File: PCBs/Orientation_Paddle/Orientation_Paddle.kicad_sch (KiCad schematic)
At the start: 46 parts

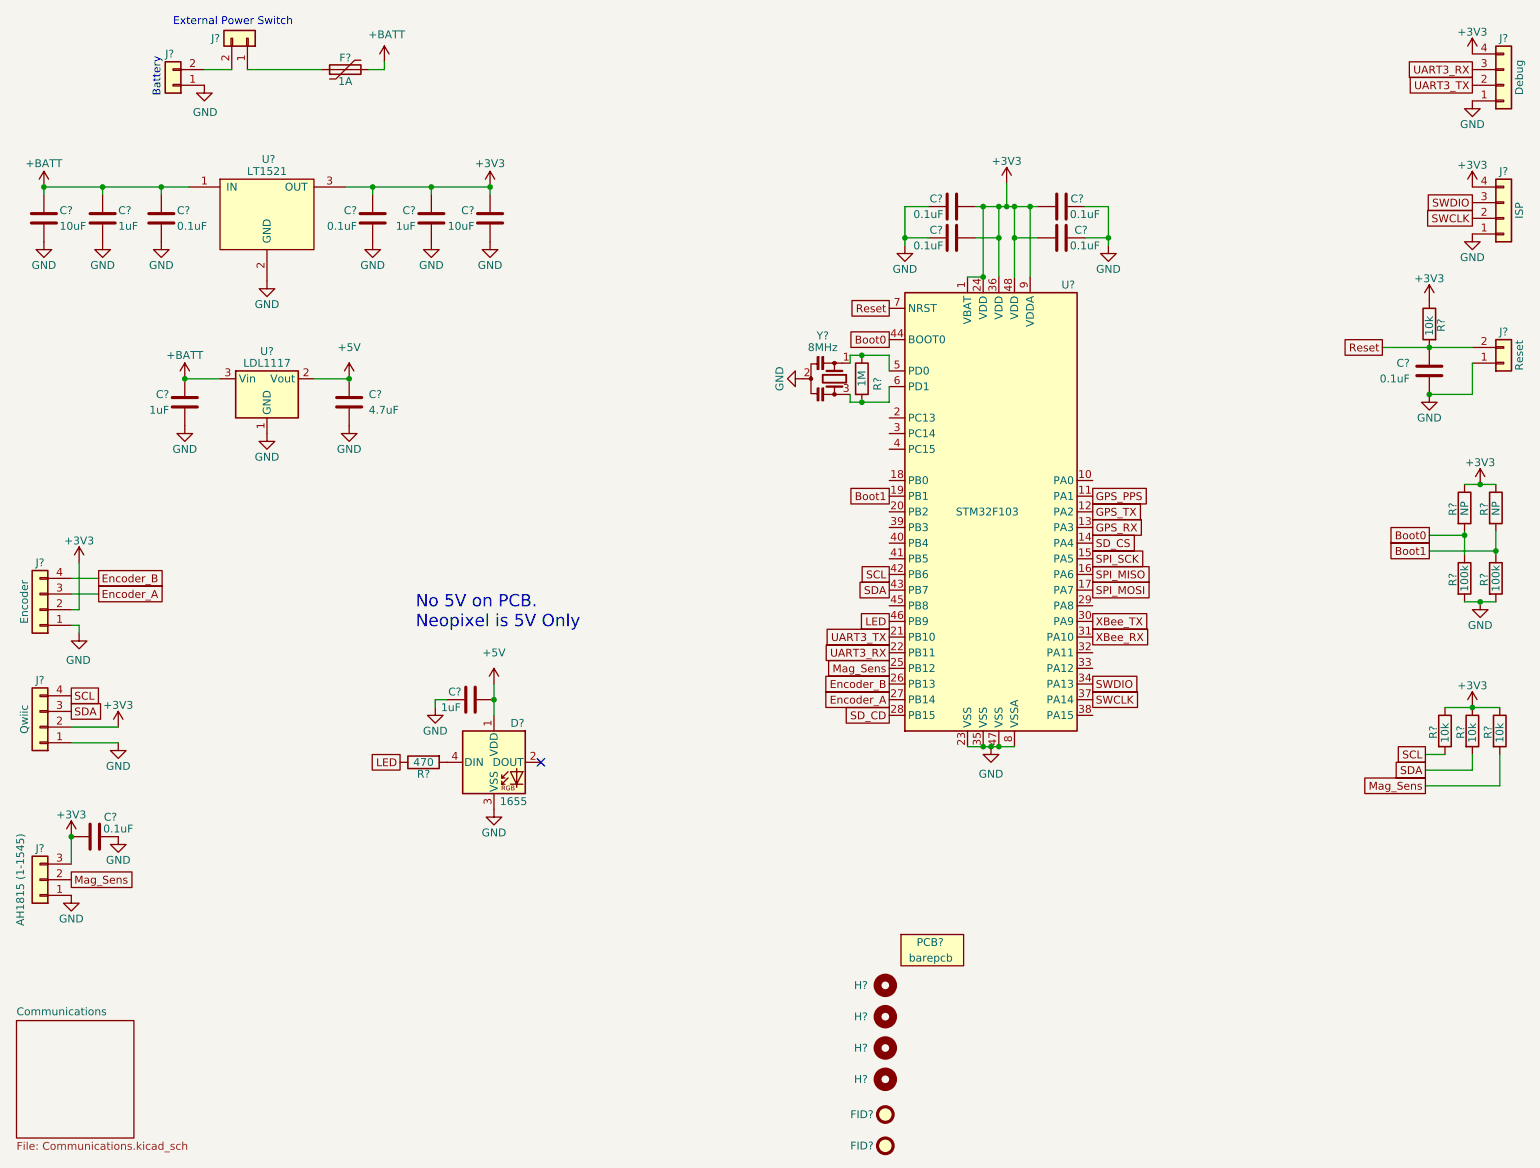
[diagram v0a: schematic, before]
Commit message: Updated Ori. Paddle Schematic with Final Revisions
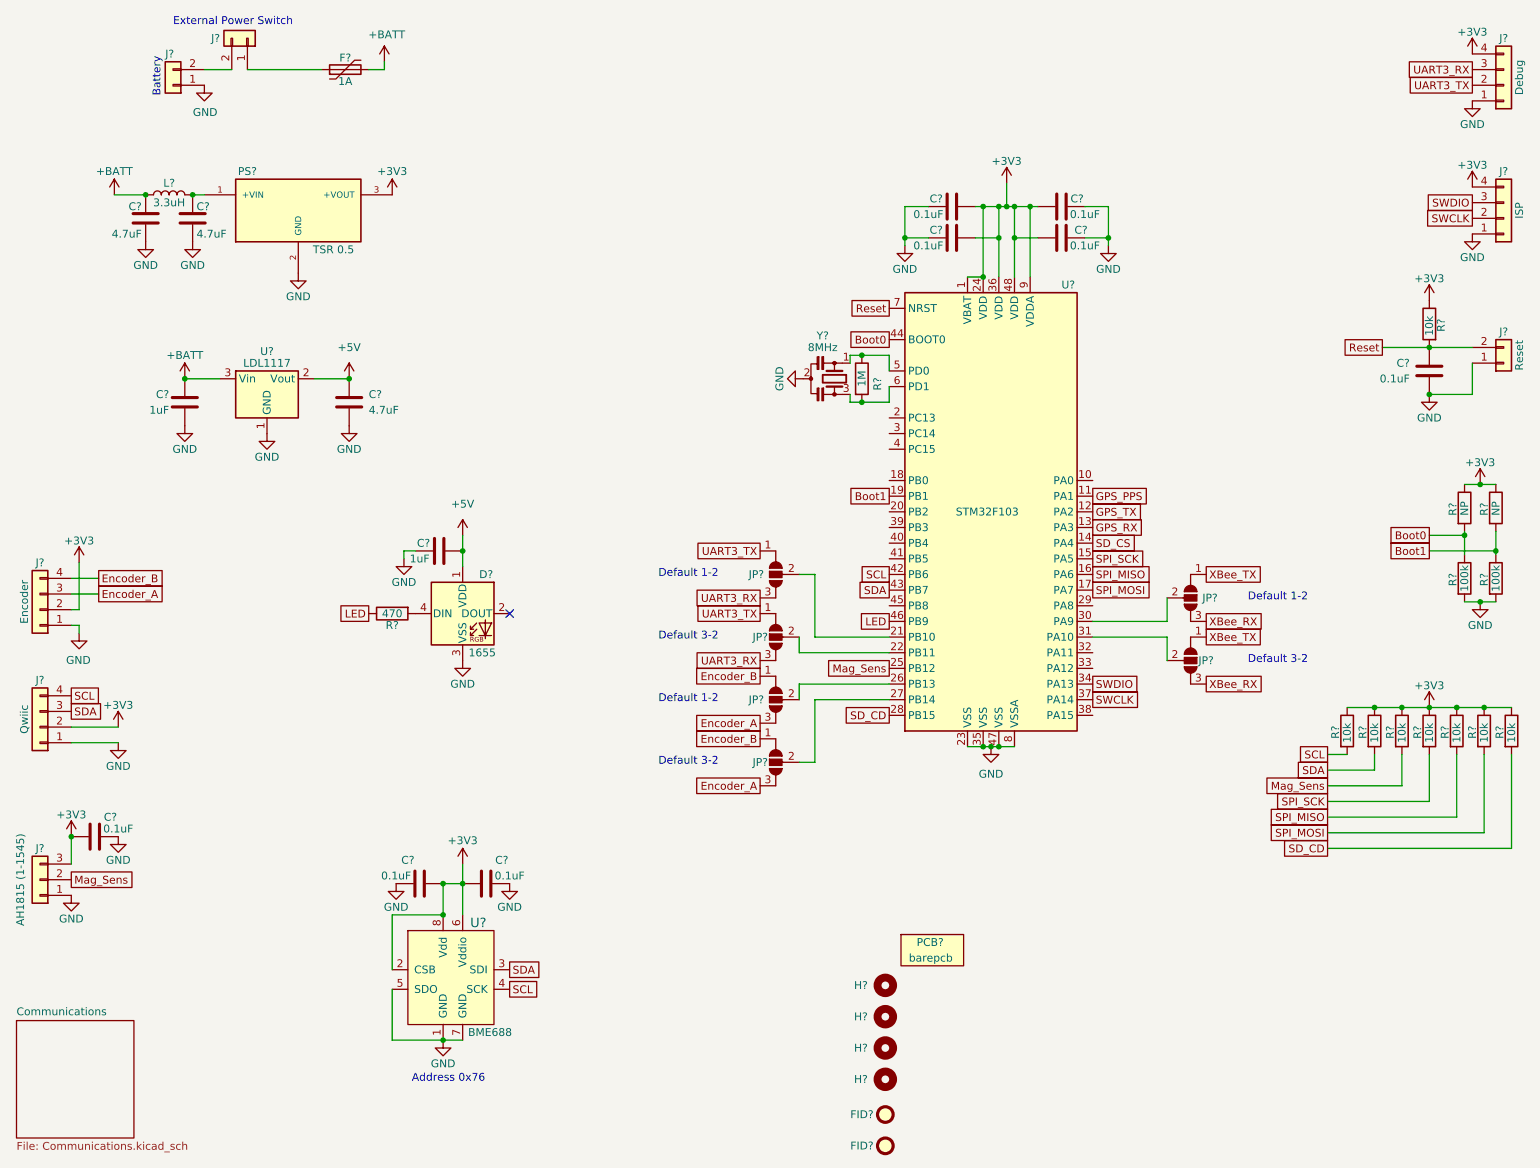
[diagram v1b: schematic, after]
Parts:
- removed C? (x2): 1-0000007, capacitors_0603:1-0000007, symbol capacitors_0603:1-0000007
- removed C? (x2): 1-0000005, capacitors_0603:1-0000005, symbol capacitors_0603:1-0000005
- removed C? (x2): 1-0000018, capacitors_0603:1-0000018, symbol capacitors_0603:1-0000018
- removed U?: 1-0000196, regulators:1-0000196, symbol regulators:1-0000196
- added C? (x2): 1-0000136, capacitors_1206:1-0000136, symbol capacitors_1206:1-0000136
- added C? (x2): 1-0000007, capacitors_0603:1-0000007, symbol capacitors_0603:1-0000007
- added JP? (x6): SolderJumper_3_Open, Jumper:SolderJumper-3_P1.3mm_Open_RoundedPad1.0x1.5mm_NumberLabels, symbol Jumper:SolderJumper_3_Open
- added L?: 1-0000931, inductors:1-0000931, symbol inductors:1-0000931
- added PS?: 1-0000727, dc_dc_converters:1-0000727, symbol dc_dc_converters:1-0000727
- added R? (x4): 1-0000010, resistors_0603:1-0000010, symbol resistors_0603:1-0000010
- added U?: 1-0001471, sensors:1-0001471, symbol sensors:1-0001471
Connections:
- net +3V3: now also C?.1, C?.2, PS?.3 (+VOUT), R?.1, R?.1, R?.1, R?.1, U?.2 (CSB), U?.6 (Vddio), U?.8 (Vdd)
- net +BATT: now also C?.1, L?.1
- net Encoder_A: now also JP?.3 (B), JP?.3 (B); no longer U?.27 (PB14)
- net Encoder_B: now also JP?.1 (A), JP?.1 (A); no longer U?.26 (PB13)
- net GND: now also C?.1, C?.2, C?.2, C?.2, PS?.2 (GND), U?.1 (GND), U?.5 (SDO), U?.7 (GND)
- net SCL: now also U?.4 (SCK)
- net SDA: now also U?.3 (SDI)
- net SD_CD: now also R?.2
- net SPI_MISO: now also R?.2
- net SPI_MOSI: now also R?.2
- net SPI_SCK: now also R?.2
- net UART3_RX: now also JP?.3 (B), JP?.3 (B); no longer U?.22 (PB11)
- net UART3_TX: now also JP?.1 (A), JP?.1 (A); no longer U?.21 (PB10)
- net XBee_RX: now also JP?.3 (B), JP?.3 (B); no longer U?.31 (PA10)
- net XBee_TX: now also JP?.1 (A), JP?.1 (A); no longer U?.30 (PA9)
- new net: C?.1, L?.2, PS?.1 (+VIN)
- new net: JP?.2 (C), U?.31 (PA10)
- new net: JP?.2 (C), U?.27 (PB14)
- new net: JP?.2 (C), U?.21 (PB10)
- new net: JP?.2 (C), U?.30 (PA9)
- new net: JP?.2 (C), U?.22 (PB11)
- new net: JP?.2 (C), U?.26 (PB13)
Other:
- note added: "Address 0x76"
- note added: "Default 1-2"
- note added: "Default 3-2"
- note removed: "No 5V on PCB. Neopixel is 5V Only"
- moved on the sheet: C?, D?, R?

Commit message: Orientation Paddle Initial PCB Layout
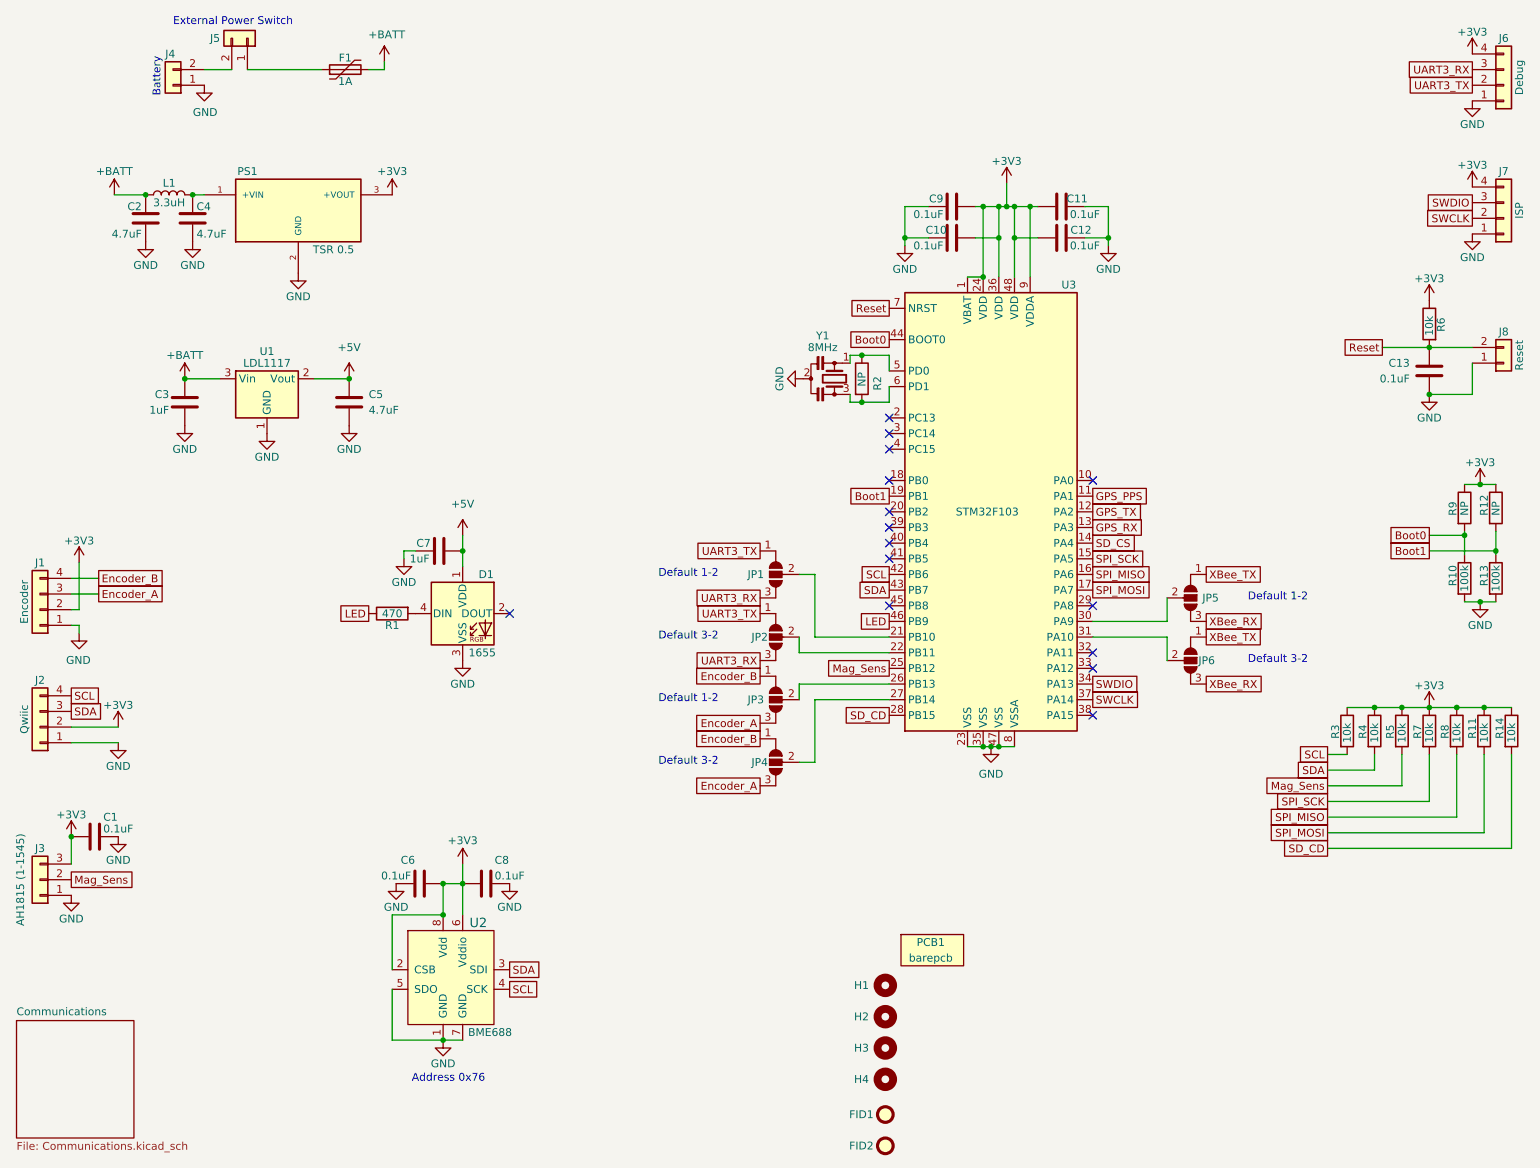
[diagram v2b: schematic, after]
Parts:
- PCB1: renamed from PCB?; Internal Part Number 0-0000000 -> 3-0000205; Populated 0 -> 1
- R2: renamed from R?; PValue 1M -> NP; Populated 1 -> 0
- gave numbers to parts that had none: 54
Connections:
- no-connect marks 1 -> 15
